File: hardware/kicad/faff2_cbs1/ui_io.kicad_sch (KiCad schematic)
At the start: 40 parts, among them J901 BTN EXT, J902 SMA Jack, J903 J-LIM, SW901 PTS526, SW902 PTS526, SW903 PTS526, SW904 PTS526, U901 SN74LVC1G17, U902 SN74LVC1G11

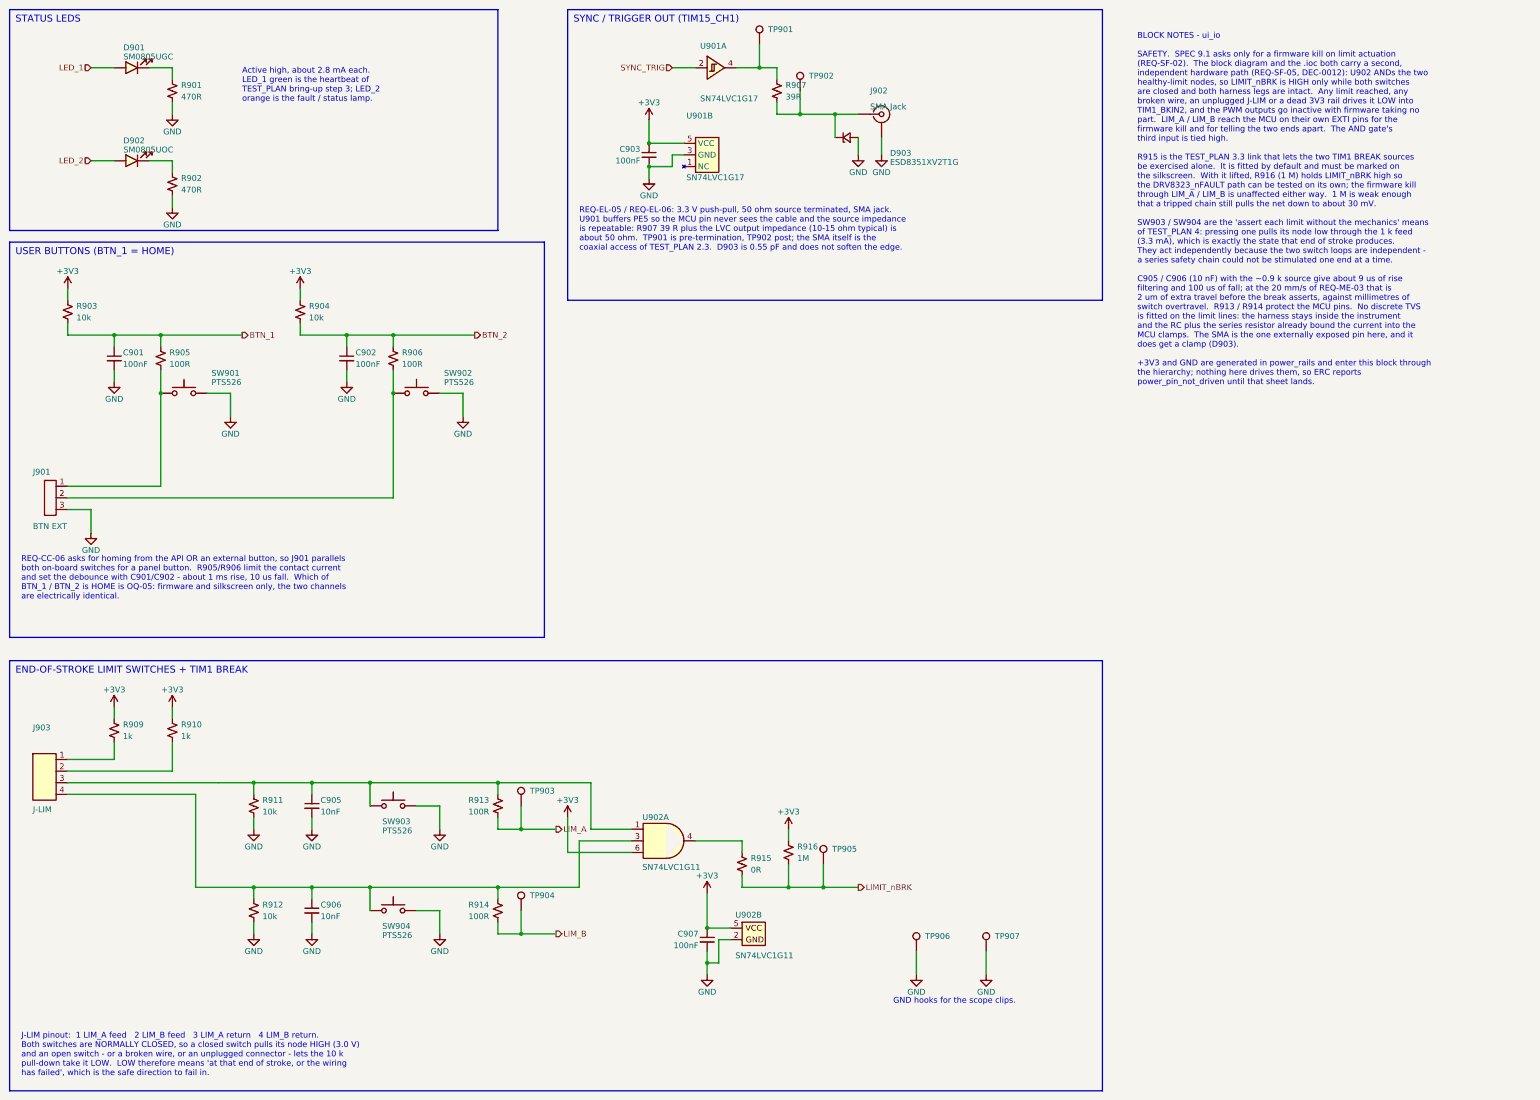
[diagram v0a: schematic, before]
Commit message: review r1: dissolve test_debug into mcu, split the 24 MHz clock, A2 mcu, ui_io flow
Captain's review, three batches, all landing on mcu.kicad_sch so they ship together.

test_debug.kicad_sch is deleted. Its three blocks moved onto the sheet they serve:
H the SWD + USART3 debug header, J the rail probe header, K the GND hooks - all on
mcu, renumbered into the 10xx range (J401->J1003, R401/402->R1013/1014, J402->J1004,
TP401..406->TP1006..1011, #PWR401..414->#PWR1051..1064). The six SWD/USART3 nets were
shared only with mcu, so they are sheet-local labels now and their twelve sheet pins
came off the root. Nine blocks; pages renumber 2..10 and the refdes ranges become a
fixed table with 4xx retired. Standing rule written into AGENTS.md: test coverage
lives on the circuit page it covers, never its own sheet.

The shared 24 MHz reference is gone. The USB3320 gets its own crystal on REFCLK/XO
(Y1002 ECS-240-12-23G-JGN-TR, 27 pF C0G load caps sized from DS Table 4-11) in a new
block C; the STM32 keeps its own oscillator, minus R1004 and the fan-out. A bare
crystal on the STM32 is impossible without an .ioc change (PH1-OSC_OUT unallocated,
REQ-AR-16), so it stays a driven clock - the two domains now share nothing.

mcu is A2 and re-laid, and all 47 hierarchical labels are right-justified so the
names align outside the wire instead of running into the pin numbers. Net labels
left alone.

ui_io is graphical only, netlist byte-identical: R907 and R915 lie along the signal
(pre-rotated variants in the new faff2_passives.kicad_sym - never an instance
rotation), D903 shunts straight down, and the LIM_A / LIM_B exits are clear of the
+3V3 riser that ran through the LIM_A label.

Verified: ERC 0 errors / 0 warnings at --severity-all, nothing suppressed; netlist
equivalent net-for-net apart from the four rows of the authorised clock change;
411 components, 253 nets, all footprints resolving; overlap checker clean on every
sheet this branch touched. Review PDF deliberately not regene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
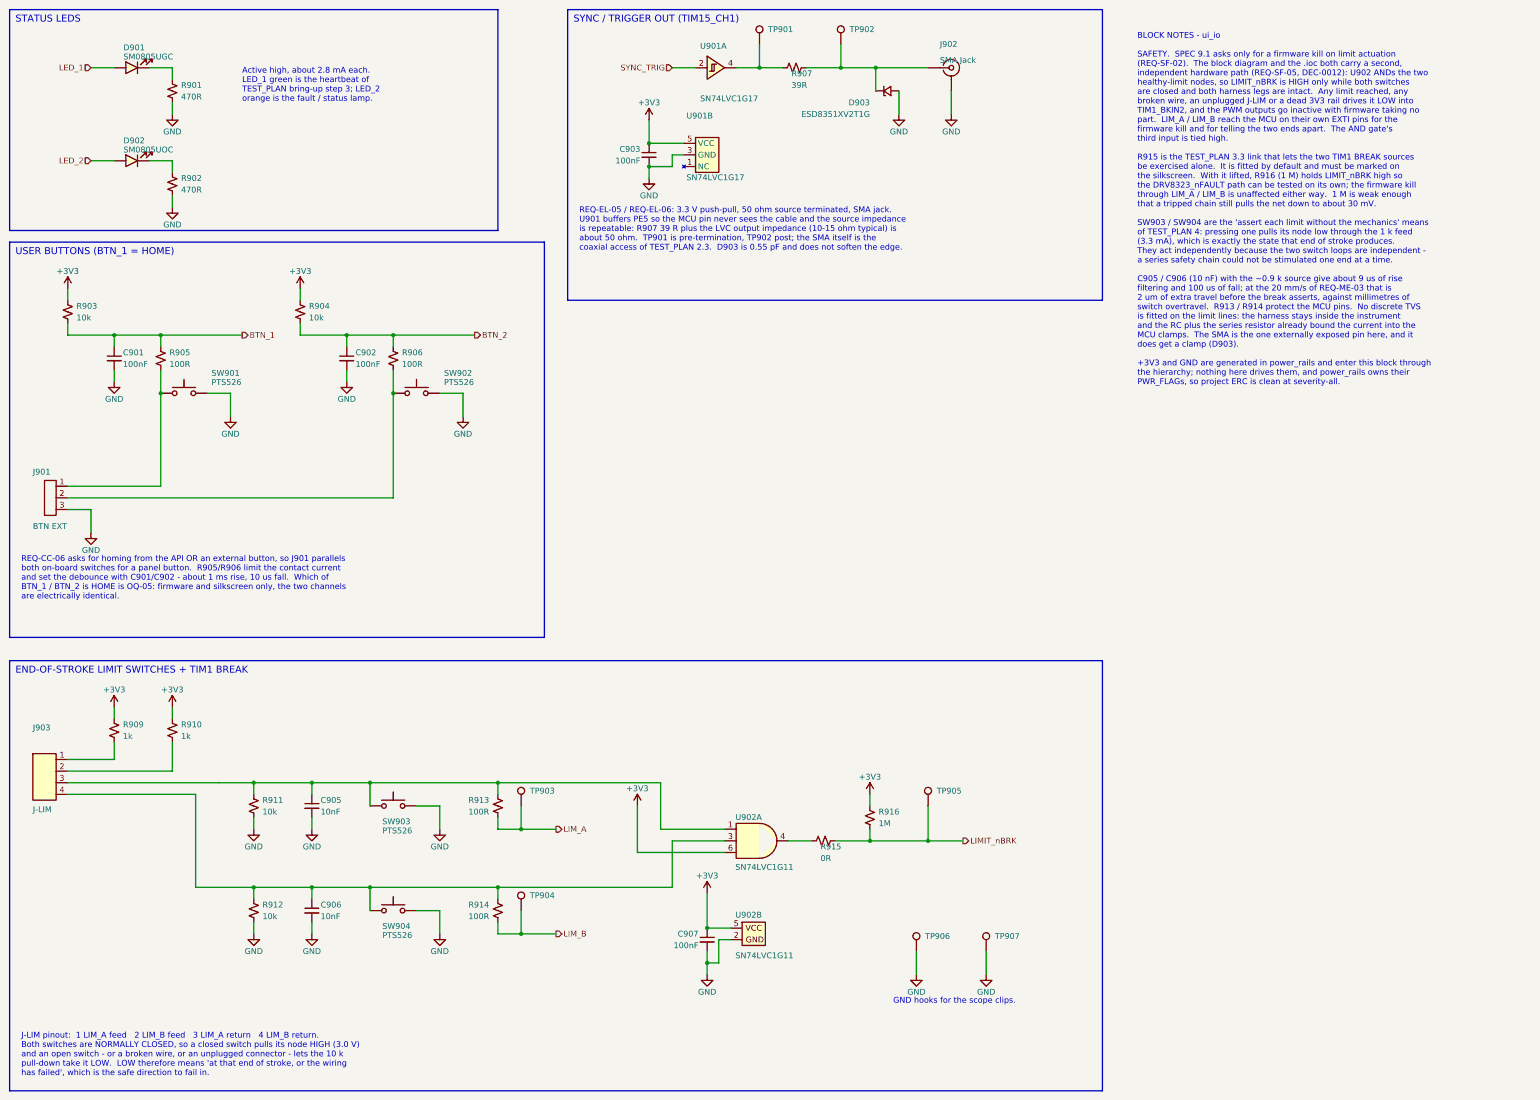
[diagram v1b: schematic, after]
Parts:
- R907: symbol Amodo_Resistors:RES_TF_39R_0603 -> faff2_passives:RES_TF_39R_0603_H
- R915: symbol Amodo_Resistors:RES_TF_0R_0603 -> faff2_passives:RES_TF_0R_0603_H
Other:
- moved on the sheet: D903, J902, R907, R915, R916, TP902, TP905, U902A

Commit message: review r1 final sweep: power labels, TP silkscreen names, text overlaps
The captain's design-wide pass, run once the per-sheet batches had landed.
Presentation only: ERC 0 errors / 0 warnings at severity-all, 404 components,
251 nets, and every per-net node set identical to the pre-sweep export.

  power labels   92 rail names were hidden on loadcell_afe, motor_drive and
                 temp_sense - all 285 power symbols now read, placed to the
                 house pattern (GND below the symbol, rail arrows above)
  test points    66 of 83 still carried the library default "TestPoint". All
                 83 now name what they measure, from the net they actually
                 land on in the netlist; longest is 5 characters
  text overlap   16 collisions cleared design-wide, four of them sub-millimetre
                 ones the bundled checker passes because it under-measures text
  GND upside down  none - 0 of 285 power symbols is rotated or mirrored
  graphic/wire   one: power_rails block D's bottom border lay along the last
                 PWR_FLAG's wire; the flag column moved up 2.54

The overlap checker turns out to have three separable blind spots, each settled
here by measuring a render rather than by reading the format: it grows every
text field rightward regardless of justify/mirror/180-rotation, so its box is a
mirror image of the truth for those and it both invents and misses collisions;
it measures text at ~1.06 mm per character where the real advance is ~1.19; and
it reflects a rotated symbol's body about the origin. tools/sch_geom.py models
all three correctly and the design is clean under it design-wide. Two of that
model's own rules - notes growing up from their anchor, and labels taking no
180-degree justify flip - were bugs of mine that the checker caught first. The
render is what settles it; neither tool is authoritative alone.

Placement is searched rather than guessed: 177 newly visible fields are tried
against every wire, block border, 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
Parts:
- TP901: value TestPoint -> SYNC
- TP902: value TestPoint -> SYNCO
- TP903: value TestPoint -> LIM_A
- TP904: value TestPoint -> LIM_B
- TP905: value TestPoint -> nBRK
- TP906, TP907: value TestPoint -> GND
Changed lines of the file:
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@@
 			)
 		)
-		(property "Value" "TestPoint"
-			(at 179.0700 15.2400 0)
+		(property "Value" "SYNC"
+			(at 180.97 19.42 0)
 			(effects
 				(font
 					(size 1.27 1.27)
 				)
-				(hide yes)
+				(justify left)
 			)
 		)
@@
 			)
 		)
-		(property "Value" "TestPoint"
-			(at 196.85 15.24 0)
+		(property "Value" "SYNCO"
+			(at 198.75 19.42 0)
 			(effects
 				(font
 					(size 1.27 1.27)
 				)
-				(hide yes)
+				(justify left)
 			)
 		)
@@
 			)
 		)
-		(property "Value" "TestPoint"
-			(at 127.0000 181.6100 0)
+		(property "Value" "LIM_A"
+			(at 128.9 185.79 0)
 			(effects
 				(font
 					(size 1.27 1.27)
 				)
-				(hide yes)
+				(justify left)
 			)
 		)
@@
 			)
 		)
-		(property "Value" "TestPoint"
-			(at 127.0000 204.4700 0)
+		(property "Value" "LIM_B"
+			(at 128.9 208.65 0)
 			(effects
 				(font
 					(size 1.27 1.27)
 				)
-				(hide yes)
+				(justify left)
 			)
 		)
@@
 			)
 		)
-		(property "Value" "TestPoint"
-			(at 215.9 181.61 0)
+		(property "Value" "nBRK"
+			(at 217.8 185.79 0)
 			(effects
 				(font
 					(size 1.27 1.27)
 				)
-				(hide yes)
+				(justify left)
 			)
 		)
@@
 			)
 		)
-		(property "Value" "TestPoint"
-			(at 213.3600 213.3600 0)
+		(property "Value" "GND"
+			(at 215.26 217.54 0)
 			(effects
 				(font
 					(size 1.27 1.27)
 				)
-				(hide yes)
+				(justify left)
 			)
 		)
@@
 			)
 		)
-		(property "Value" "TestPoint"
-			(at 228.6000 213.3600 0)
+		(property "Value" "GND"
+			(at 230.5 217.54 0)
 			(effects
 				(font
 					(size 1.27 1.27)
 				)
-				(hide yes)
+				(justify left)
 			)
 		)

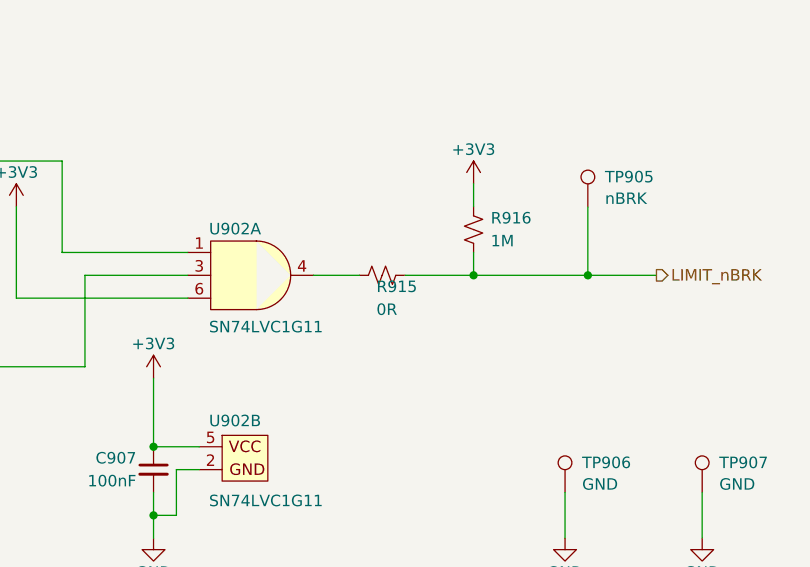
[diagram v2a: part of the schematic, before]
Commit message: review r2 items 4-7: four per-sheet placement fixes
  4  linear_encoder - U601A's GND body ended at y=166.37 and U601E's +3V3 body
     began at exactly 166.37, so the two flags were touching. The whole U601E
     group drops 7.62 - unit, both flags, four wires, and the no_connect on its
     unused output, which does NOT ride with the symbol: ERC caught that as
     pin_not_connected plus a dangling no-connect the first time round.
  5  temp_sense - C704/C705's grounds sat 0.6 mm above the REFP row with
     TP705's reference on the row itself; the caps and grounds move up 5.08.
     Three verticals ran through the block title, so it is shortened to
     "CHANNEL 2 FILTER + SHARED REF", which at size 1.778 ends at x=135.9 and
     clears the leftmost of them at 137.16.
  6  ui_io - R915's reference sat on its own body. It is the horizontal 0R
     variant but its fields were still on the vertical pattern; moved to the
     _H symbol's own pattern.
  7  motor_drive - #PWR1109/#PWR1110 bodies ended exactly on the block border
     and their GND text was outside the box entirely. Both move up to 138.43.

ERC 0 errors / 0 warnings at severity-all; 412 components, 259 nets, node sets
identical - all four are placement only.

Co-Authored-By: Claude Opus 5 <noreply@anthropic.com>
Claude-Session: https://claude.ai/code/session_01PFWfwT8RZc8Zqn8vgZxV8j
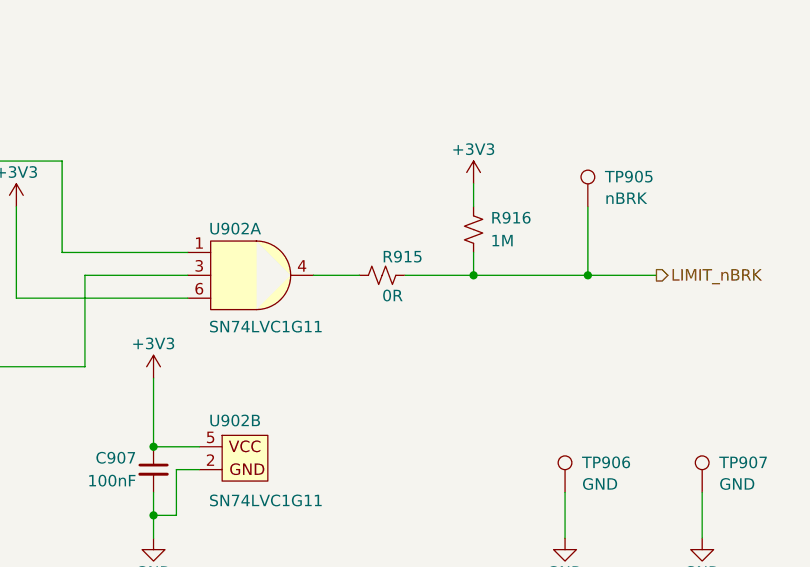
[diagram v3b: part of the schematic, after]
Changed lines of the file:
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@@
 		(dnp no)
 		(property "Reference" "R915"
-			(at 192.405 195.58 0)
+			(at 193.04 192.28 0)
 			(effects
 				(font
@@
 		)
 		(property "Value" "0R"
-			(at 192.405 198.12 0)
+			(at 193.04 196.6 0)
 			(effects
 				(font
